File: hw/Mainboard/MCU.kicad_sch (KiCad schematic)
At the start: 46 parts, among them J13 Micro_SD, J14 USB2.0_HOST_TYPE_C, J15 DEBUG, J16 MCU, J17 BOOTSEL, J22 MENU, SW2 RUN, SW3 MENU, U14 RP2040, U16 W25Q128JVS, Y1 12 MHz

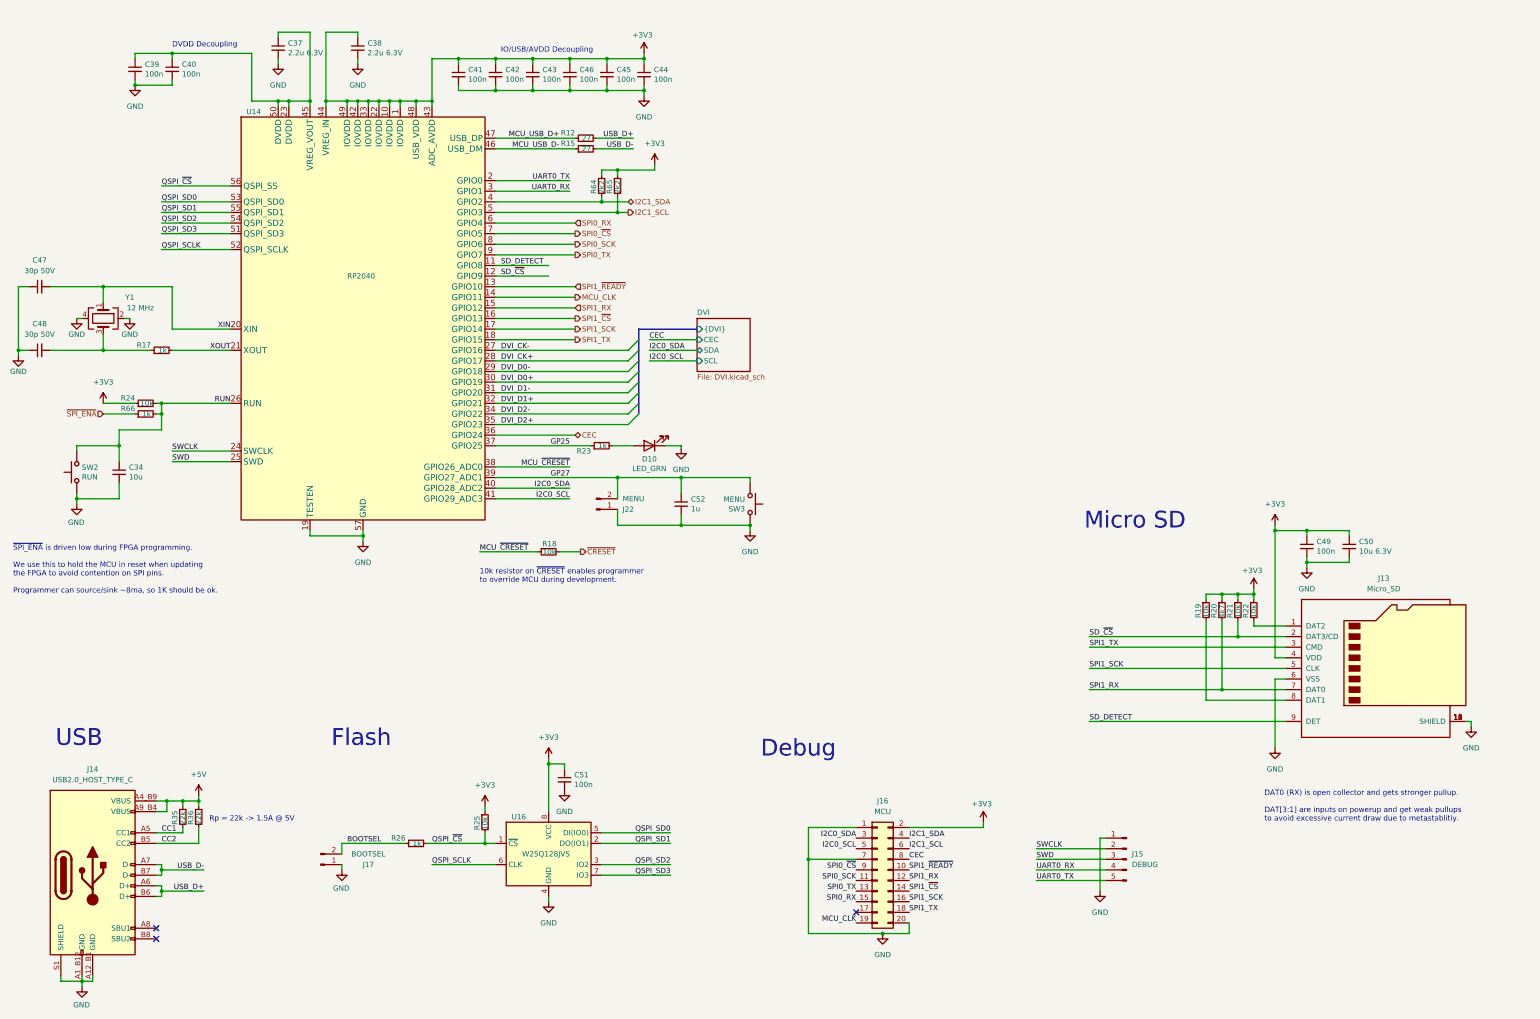
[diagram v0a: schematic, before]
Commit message: hw: move microSD to it's own sheet
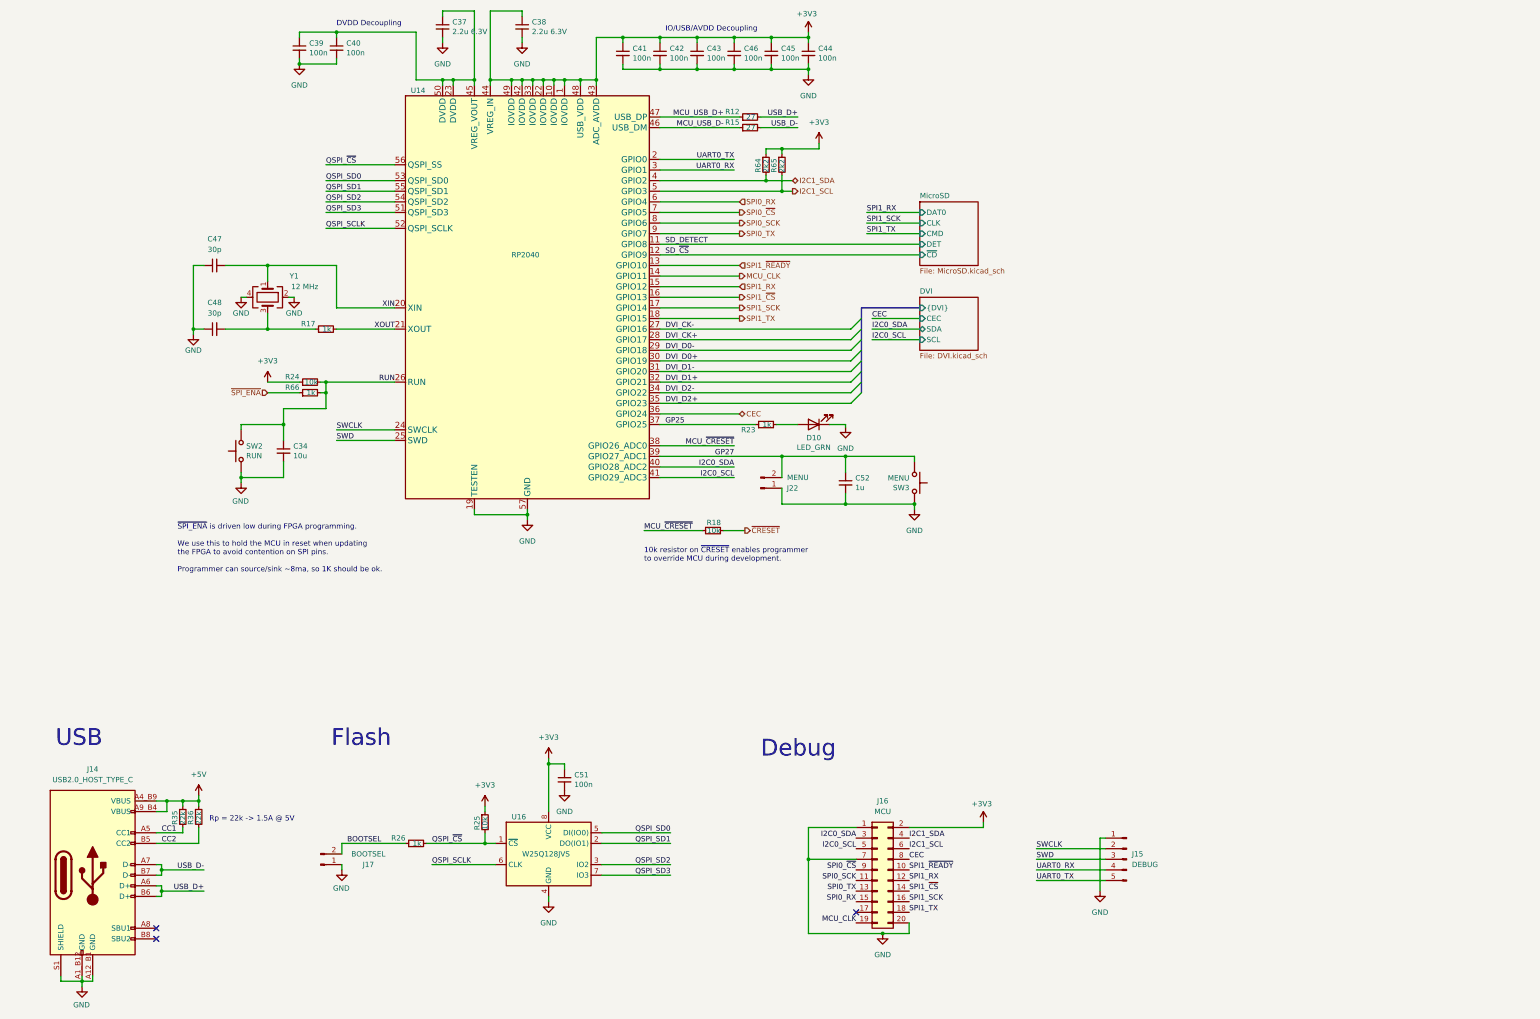
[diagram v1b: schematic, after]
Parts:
- removed C49: 100n, Capacitor_SMD:C_0402_1005Metric, symbol Device:C_Small
- removed C50: 10u 6.3V, Capacitor_SMD:C_0402_1005Metric, symbol Device:C_Small
- removed J13: Micro_SD, JLCPCB:SIM-SMD_8P-1040310811, symbol Connector:Micro_SD_Card_Det
- removed R19, R21, R22: 10k, Resistor_SMD:R_0402_1005Metric, symbol Device:R_Small
- removed R20: 4k7, Resistor_SMD:R_0402_1005Metric, symbol Device:R_Small
- C47, C48: value 30p 50V -> 30p
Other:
- added sheet MicroSD (MicroSD.kicad_sch)
- note removed: "DAT0 (RX) is open collector and gets stronger pullup. DAT[3:1] are inputs on powerup and get weak pullups to avoid excessive current draw due to metastablitiy."
- note removed: "Micro SD"
- moved on the sheet: C34, C37, C38, C39, C40, C41, C42, C43, C44, C45, C46, C47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

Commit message: hw: move usb to it's own sheet
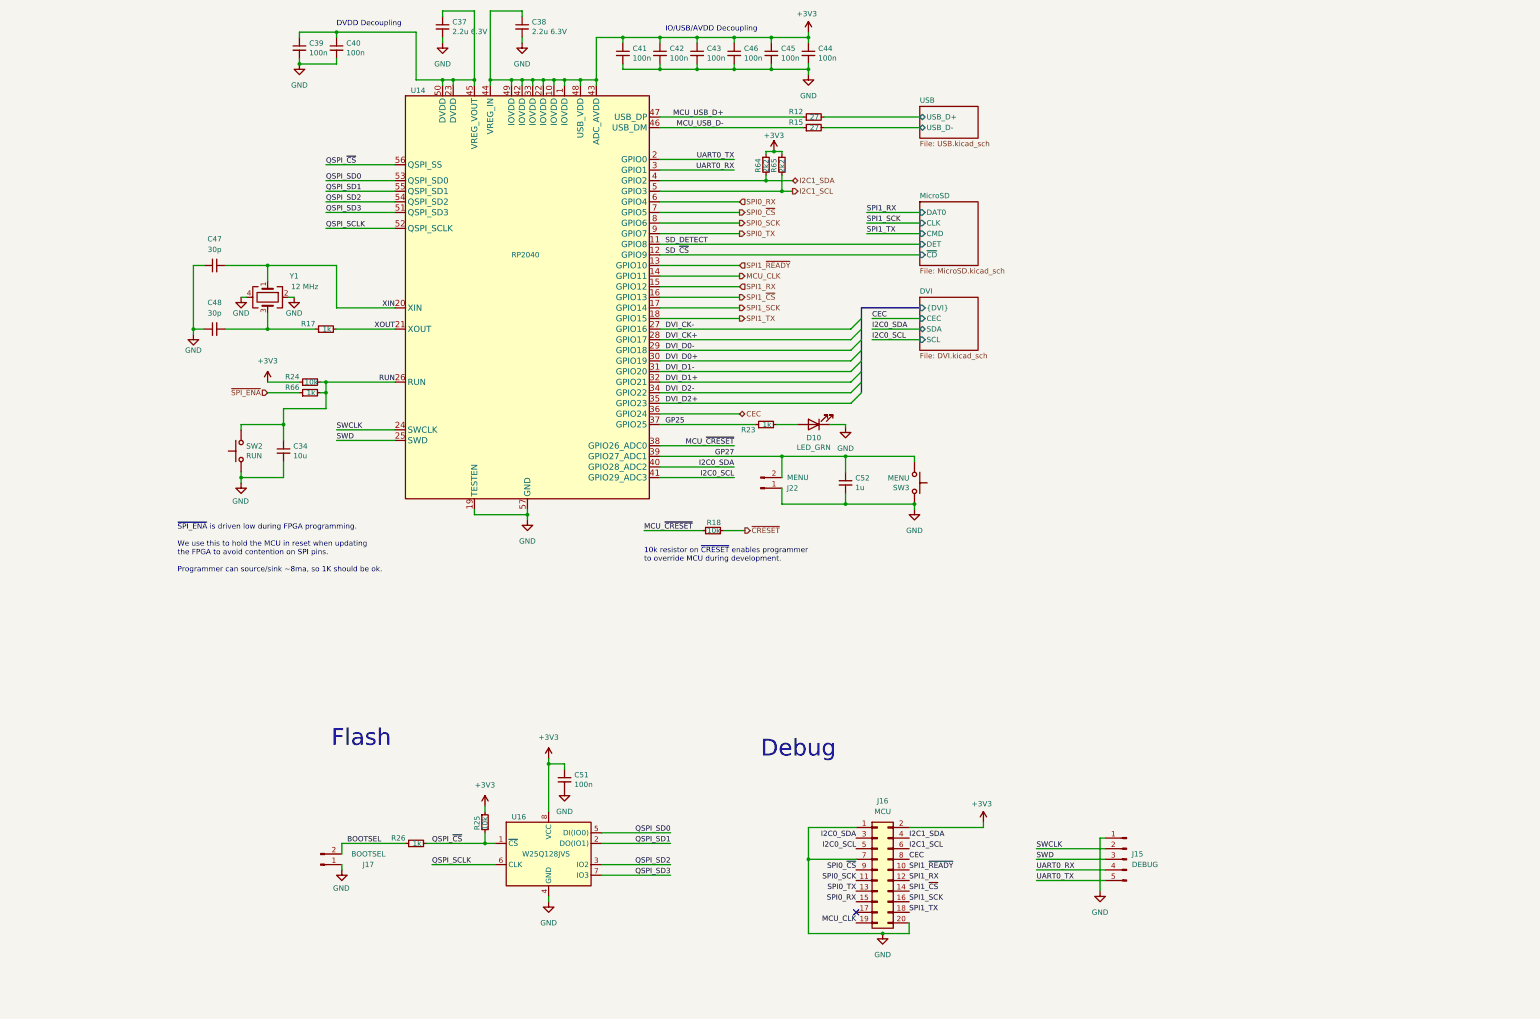
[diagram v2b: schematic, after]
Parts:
- removed J14: USB2.0_HOST_TYPE_C, JLCPCB:USB-C_SMD-TYPE-C-31-M-12, symbol JLCPCB:USB_C_Receptacle_USB2.0
- removed R35, R36: 22k, Resistor_SMD:R_0402_1005Metric, symbol Device:R_Small
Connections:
- net USB_D+ renamed USB/USB_D+
- net USB_D- renamed USB/USB_D-
- no-connect marks 3 -> 1
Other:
- added sheet USB (USB.kicad_sch)
- note removed: "Rp = 22k -> 1.5A @ 5V"
- note removed: "USB"
- moved on the sheet: R12, R15

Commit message: hw: move flash to separate sheet
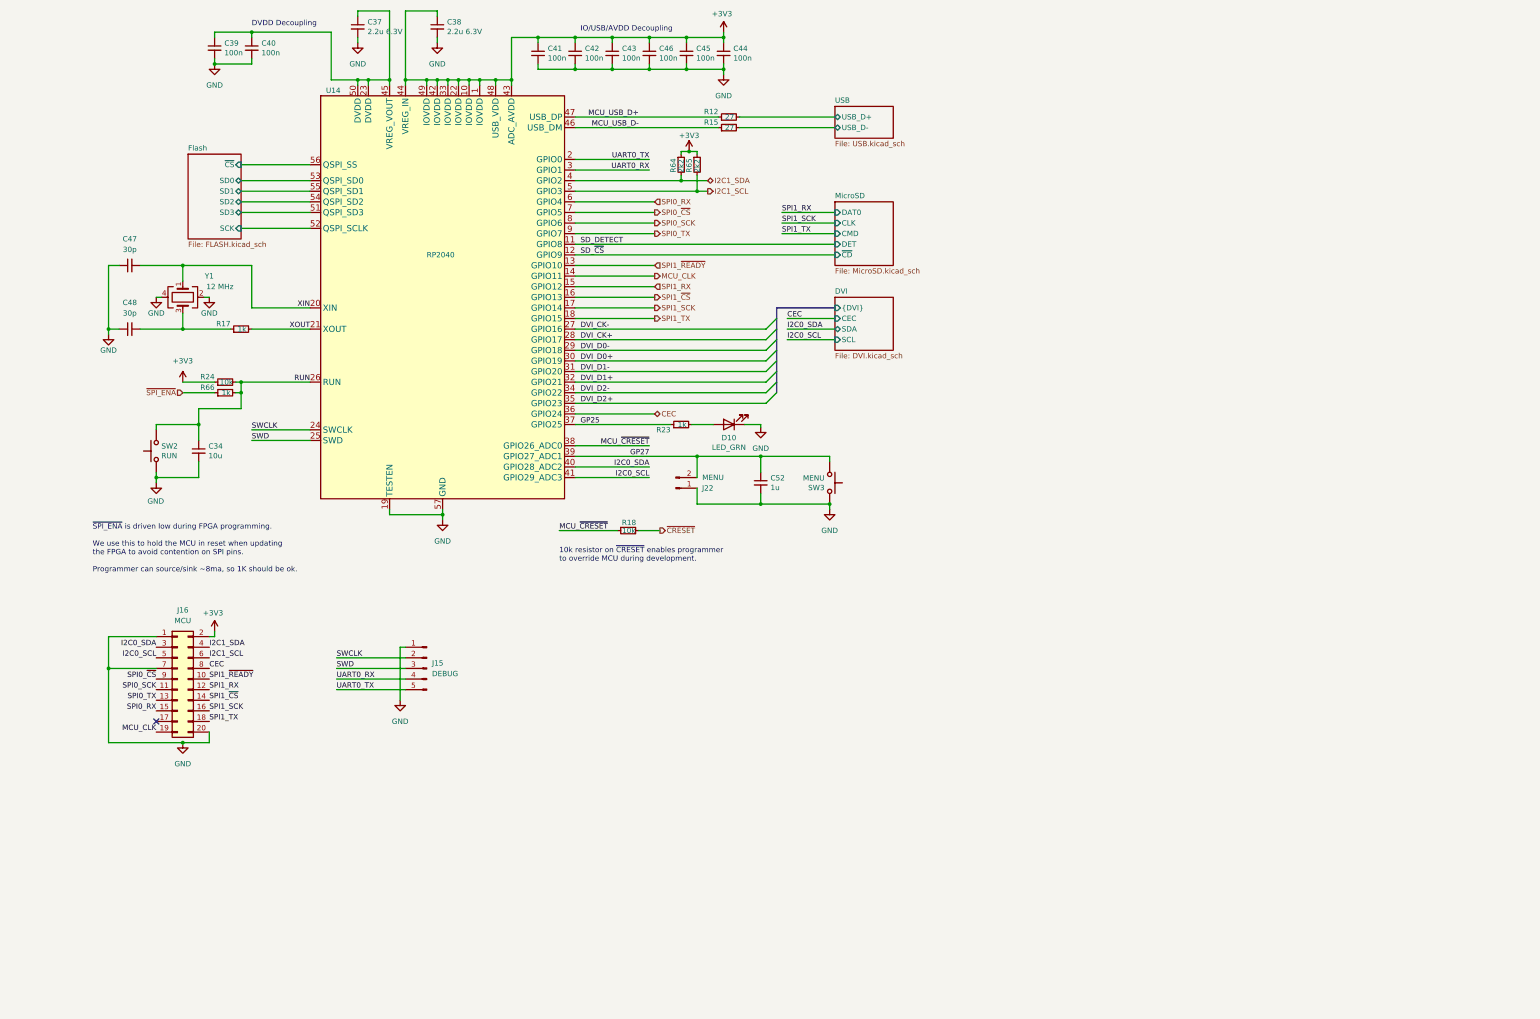
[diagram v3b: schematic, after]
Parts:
- removed C51: 100n, Capacitor_SMD:C_0402_1005Metric, symbol Device:C_Small
- removed J17: BOOTSEL, Connector_PinHeader_2.54mm:PinHeader_1x02_P2.54mm_Vertical, symbol Connector:Conn_01x02_Male
- removed R25: 10k, Resistor_SMD:R_0402_1005Metric, symbol Device:R_Small
- removed R26: 1k, Resistor_SMD:R_0402_1005Metric, symbol Device:R_Small
- removed U16: W25Q128JVS, Package_SO:SOIC-8_5.23x5.23mm_P1.27mm, symbol Memory_Flash:W25Q128JVS
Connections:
- net QSPI_SCLK renamed Flash/SCK
- net QSPI_SD0 renamed Flash/SD0
- net QSPI_SD1 renamed Flash/SD1
- net QSPI_SD2 renamed Flash/SD2
- net QSPI_SD3 renamed Flash/SD3
- net QSPI_~{CS} renamed Flash/~{CS}
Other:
- added sheet Flash (FLASH.kicad_sch)
- note removed: "Debug"
- note removed: "Flash"
- moved on the sheet: C34, C37, C38, C39, C40, C41, C42, C43, C44, C45, C46, C47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

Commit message: hw: wip
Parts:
- removed J15: DEBUG, Connector_PinHeader_2.54mm:PinHeader_1x05_P2.54mm_Vertical, symbol Connector:Conn_01x05_Male
- added PT1, PT2: PowerTie_2, PET:NetTie-2_SMD_Pad_0.4_to_0.2mm, symbol PET:PowerTie_2
- added R19, R21, R22: 33, Resistor_SMD:R_0402_1005Metric, symbol Device:R_Small
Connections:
- net +3V3: now also PT1.1; no longer C38.1, C41.1, C42.1, C43.1, C44.1, C45.1, C46.1, U14.1 (IOVDD), U14.10 (IOVDD), U14.22 (IOVDD), U14.33 (IOVDD), U14.42 (IOVDD), U14.43 (ADC_AVDD), U14.44 (VREG_IN), U14.48 (USB_VDD), U14.49 (IOVDD)
- net GND: now also PT2.1; no longer SW2.1, U14.19 (TESTEN)
- net SPI0_SCK: now also R19.1; no longer U14.8 (GPIO6)
- net SPI1_SCK: now also R22.1; no longer U14.17 (GPIO14)
- net DVDD: now reaches C37.1, C39.1, C40.1, U14.23 (DVDD), U14.45 (VREG_VOUT), U14.50 (DVDD)
- net MCU_CLK: no longer names the net of J16.19 (Pin_19)
- net MCU_CLK: no longer U14.14 (GPIO11)
- net UART0_RX renamed UART_RX
- net UART0_TX renamed UART_TX
- new net FPGA_CLK: R21.1
- new net MCU_FPGA_CLK: R21.2, U14.14 (GPIO11)
- new net MCU_IOVDD: C38.1, C41.1, C42.1, C43.1, C44.1, C45.1, C46.1, PT1.2, U14.1 (IOVDD), U14.10 (IOVDD), U14.22 (IOVDD), U14.33 (IOVDD), U14.42 (IOVDD), U14.43 (ADC_AVDD), U14.44 (VREG_IN), U14.48 (USB_VDD), U14.49 (IOVDD)
- new net MCU_SPI0_SCK: R19.2, U14.8 (GPIO6)
- new net MCU_SPI1_SCK: R22.2, U14.17 (GPIO14)
- new net MCU_TESTEN: PT2.2, U14.19 (TESTEN)
- new net PD_GND: SW2.1
- no-connect marks 1 -> 2

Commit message: wip: support 8x16 keyboard matrix
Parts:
- removed J16: MCU, Connector_PinHeader_2.54mm:PinHeader_2x10_P2.54mm_Vertical, symbol Connector_Generic:Conn_02x10_Odd_Even
- added R48, R51, R63, R67: 33, Resistor_SMD:R_0402_1005Metric, symbol Device:R_Small
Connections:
- net MCU_FPGA_CLK: now also U14.18 (GPIO15); no longer U14.14 (GPIO11)
- net SPI0_TX: now also R67.1; no longer U14.9 (GPIO7)
- net SPI0_~{CS}: now also R63.1; no longer U14.7 (GPIO5)
- net SPI1_TX: now also R48.1; no longer U14.18 (GPIO15)
- net SPI1_~{CS}: now also R51.1; no longer U14.16 (GPIO13)
- new net MCU_SPI0_TX: R67.2, U14.9 (GPIO7)
- new net MCU_SPI0_~{CS}: R63.2, U14.7 (GPIO5)
- new net MCU_SPI1_TX: R48.2, U14.14 (GPIO11)
- new net MCU_SPI1_~{CS}: R51.2, U14.16 (GPIO13)
- no-connect marks 2 -> 0
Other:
- note added: "~{SPI_ENA} is driven low during FPGA programming. We use this to hold the MCU in reset when updating the FPGA to avoid contention on SPI pins. FT2232H can source/sink ~8ma, so 1K should be ok."
- note removed: "~{SPI_ENA} is driven low during FPGA programming. We use this to hold the MCU in reset when updating the FPGA to avoid contention on SPI pins. Programmer can source/sink ~8ma, so 1K should be ok."
- moved on the sheet: R21
